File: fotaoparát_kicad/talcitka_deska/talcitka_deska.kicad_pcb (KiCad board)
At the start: 2 copper layers, 16 parts, among them J1 Conn_01x07_Pin, SW1 SW_Push, SW2 SW_Push, SW3 SW_Push, SW4 SW_Push, SW5 SW_Push

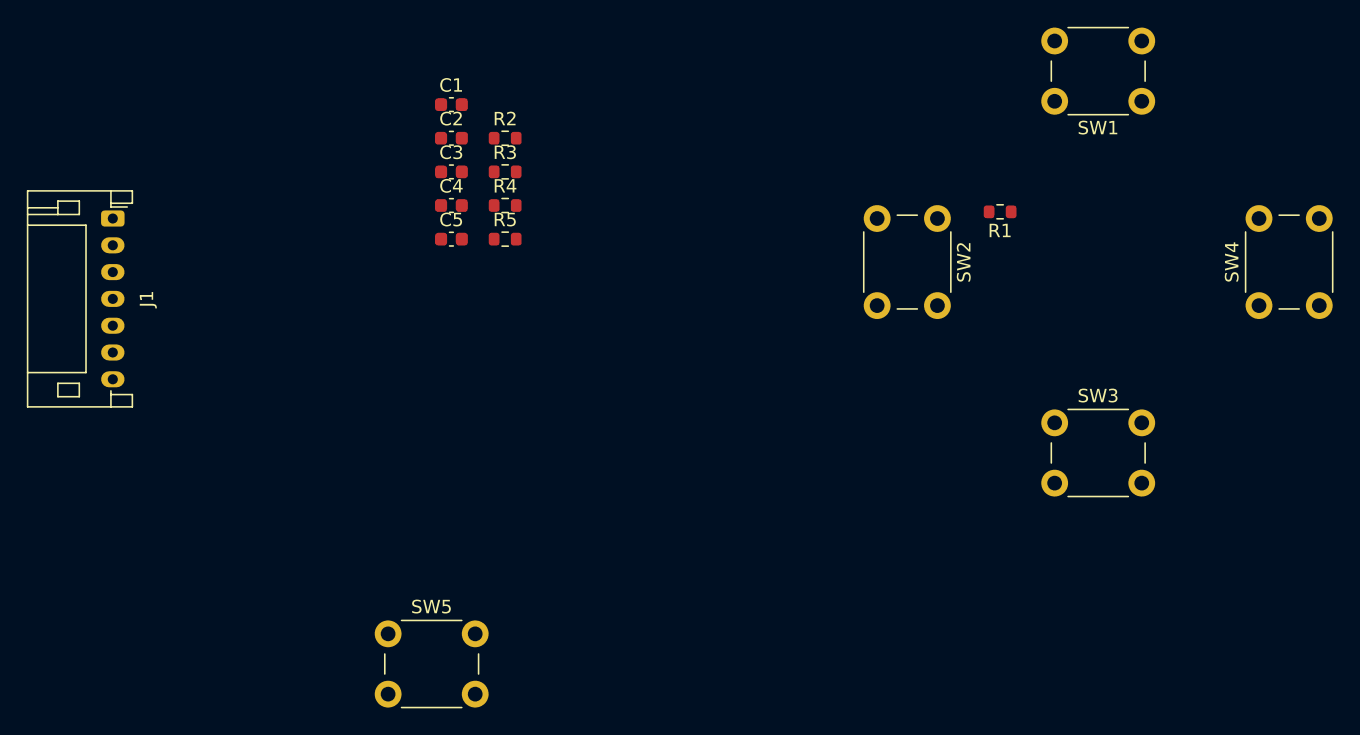
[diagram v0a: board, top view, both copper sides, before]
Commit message: Předělání powerrials,  přidání malého pcb na spousť foťáku
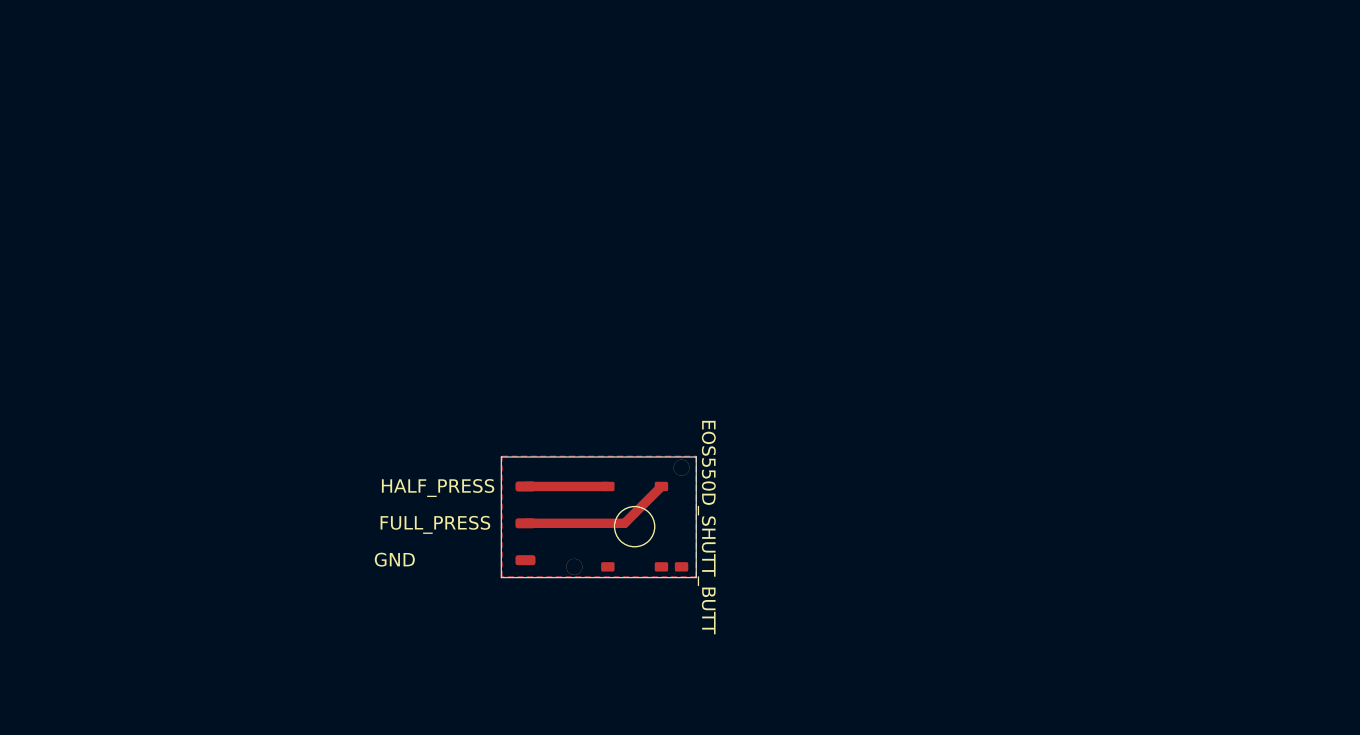
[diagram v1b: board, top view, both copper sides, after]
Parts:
- removed C1, C2, C3, C4, C5: 1uF, Capacitor_SMD:C_0603_1608Metric
- removed J1: Conn_01x07_Pin, Connector_JST:JST_PH_S7B-PH-K_1x07_P2.00mm_Horizontal
- removed R1, R2, R3, R4, R5: 10k, Resistor_SMD:R_0603_1608Metric
- removed SW1, SW2, SW3, SW4, SW5: SW_Push, Button_Switch_THT:SW_PUSH_6mm_H5mm
- added ?: , , F.Cu at (162.4, 96.0)
- added EOS550D_SHUTT_BUTT: EOS_550D_SHUTTER_BUTTON, vlastni_footprinty:EOS_550D_SHUTTER_BUTTON, F.Cu at (166.9, 93.0)
- added FULL_PRESS: SolderWirePad_1x01_SMD_1.5x3mm, Connector_Wire:SolderWirePad_1x01_SMD_1.5x3mm, F.Cu at (158.8, 92.8)
- added GND: SolderWirePad_1x01_SMD_1.5x3mm, Connector_Wire:SolderWirePad_1x01_SMD_1.5x3mm, F.Cu at (158.8, 95.5)
- added HALF_PRESS: SolderWirePad_1x01_SMD_1.5x3mm, Connector_Wire:SolderWirePad_1x01_SMD_1.5x3mm, F.Cu at (158.8, 90.0)
- added REF**: Pin_D1.0mm_L10.0mm_LooseFit, Connector_Pin:Pin_D1.0mm_L10.0mm_LooseFit, F.Cu at (170.4, 88.6)
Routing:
- net (no net): track 0.00 -> 17.4 mm
- added copper zone on F.Cu, net GND
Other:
- board outline added: 14.6 x 9 mm
